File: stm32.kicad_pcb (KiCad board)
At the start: 4 copper layers, 50 x 100 mm, 165 parts, among them CN1 SM04B-SRSS-TB (LF)(SN), CN2 SM04B-SRSS-TB (LF)(SN), CN3 SM04B-SRSS-TB (LF)(SN), J1 PZ254V-11-03P_C2937625, J2 PZ254V-11-03P_C2937625, J3 B2B-PH-SM4-TB (LF)(SN), J5 PZ254V-11-03P_C2937625, P1 TYPE-C 16PIN 2MD(073), Q1 DMG2301L-7, SW1 JS102011JCQN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

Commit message: pre placement and type c routing
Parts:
- moved P1 149.8 mm to (60.0, 128.5)
- moved D7 146.7 mm to (53.5, 125.6), turned to 90 degrees
- moved D4 142.8 mm to (73.5, 128.0), turned to -90 degrees
- moved D3 141.5 mm to (76.5, 127.8), turned to -90 degrees
- moved R35 139.6 mm to (52.5, 106.5), turned to -90 degrees
- moved D9 139.0 mm to (57.5, 121.0)
- moved D6 137.3 mm to (66.5, 127.4), turned to 90 degrees
- moved D8 136.5 mm to (61.4, 121.0), turned to 180 degrees
- moved R37 135.9 mm to (55.5, 106.5), turned to -90 degrees
- moved R7 134.7 mm to (51.8, 122.5)
- moved U6 134.1 mm to (66.5, 106.5)
- moved C7 129.8 mm to (51.5, 117.5), turned to -90 degrees
- moved U2 129.0 mm to (74.0, 123.5), turned to -90 degrees
- moved C6 128.8 mm to (51.5, 112.5), turned to 90 degrees
- moved TP2 127.9 mm to (52.5, 38.0), turned to 180 degrees
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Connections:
- C1 pad 2: +5V -> /USB/5V_INA
- C133 pad 2: +5V -> /USB/5V_INA
- C134 pad 2: +5V -> /USB/5V_INA
- R1 pad 2: +5V -> /USB/5V_INA
- R33 pad 1: /stm32_page/RGB_LEDS -> /stm32_page/RGB_LEDS_R
- R41 pad 1: /stm32_page/SWDIO -> /stm32_page/SWCLK
- U1 pad 28: /stm32_page/RGB_LEDS -> /stm32_page/RGB_LEDS_R
- U3 pad 1: +5V -> /USB/5V_INA
- U5 pad 3: Net-(U5-VIN) -> +5V
- U6 pad 1: +5V -> /USB/5V_INA
- U6 pad 10: +5V -> /USB/5V_INA
- U6 pad 12: +5V -> /USB/5V_INA
- U6 pad 14: Net-(U5-VIN) -> +5V
- U6 pad 15: Net-(U5-VIN) -> +5V
- U6 pad 16: Net-(U5-VIN) -> +5V
- U6 pad 2: +5V -> /USB/5V_INA
- U6 pad 3: +5V -> /USB/5V_INA
- U9 pad 2: /stm32_page/RGB_LEDS -> /sensors/DIN
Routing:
- net +5VP: track 0.00 -> 34.6 mm, vias 0 -> 10
- net GND: track 0.00 -> 19.1 mm, vias 0 -> 13
- net /USB/USB_TX: track 0.00 -> 14.5 mm, vias 0 -> 2
- net /USB/USB_RX: track 0.00 -> 13.6 mm, vias 0 -> 2
- net /USB/CC2: track 0.00 -> 11.6 mm
- net /USB/STAT2: track 0.00 -> 9.44 mm
- net Net-(U13-V3): track 0.00 -> 8.84 mm
- net /USB/CC1: track 0.00 -> 8.22 mm
- net /USB/STAT1: track 0.00 -> 7.70 mm
- net Net-(D3-A): track 0.00 -> 1.95 mm
- net Net-(D4-A): track 0.00 -> 1.75 mm
- added copper zone on In2.Cu, net +3V3
- added copper zone on In2.Cu, net +5V
- added copper zone on In2.Cu, net +5VP
- added copper zone on In1.Cu, net GND

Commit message: routing - type c and all 5vp+ cmp
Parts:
- moved D9 0.50 mm to (58.0, 121.0)
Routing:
- net /USB/USB_D-: track 0.00 -> 14.4 mm, vias 0 -> 2
- net /USB/USB_D+: track 0.00 -> 11.7 mm
- net GND: track 19.1 -> 22.6 mm, vias 13 -> 15

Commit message: routing all power
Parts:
- added C8: CC0603KRX7R9BB104, easyeda2kicad:C0603, F.Cu at (71.0, 108.7)
- moved D1 25.5 mm to (96.0, 130.0)
- moved R44 24.7 mm to (95.6, 110.2), turned to 180 degrees
- moved R43 23.4 mm to (93.5, 112.0), turned to 180 degrees
- moved R2 20.0 mm to (98.0, 127.0), turned to 90 degrees
- moved R3 19.0 mm to (87.5, 122.2), turned to -90 degrees
- moved R4 18.6 mm to (82.5, 124.5)
- moved R13 18.1 mm to (95.6, 108.2), turned to 180 degrees
- moved TH1 16.8 mm to (85.5, 122.2), turned to 90 degrees
- moved C2 16.3 mm to (89.0, 112.5), turned to 0 degrees
- moved R16 15.9 mm to (79.5, 127.5), turned to 90 degrees
- moved U3 14.4 mm to (90.6, 109.8), turned to -90 degrees
- moved C4 14.1 mm to (79.2, 123.0), turned to 180 degrees
- moved R8 12.7 mm to (82.5, 127.8)
- moved R9 12.7 mm to (82.5, 131.2)
- moved R1 12.6 mm to (92.6, 107.2), turned to 90 degrees
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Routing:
- net GND: track 22.6 -> 65.3 mm, vias 15 -> 36
- net /stm32_page/I2C3_SDA: track 0.00 -> 35.1 mm
- net /USB/5V_INA: track 0.00 -> 34.4 mm, vias 0 -> 9
- net /stm32_page/I2C3_SCL: track 0.00 -> 28.1 mm
- net LIPO+: track 0.00 -> 18.8 mm, vias 0 -> 6
- net /USB/VIN: track 0.00 -> 10.9 mm, vias 0 -> 4
- net +3V3: track 0.00 -> 9.68 mm, vias 0 -> 5
- net +5V: track 0.00 -> 9.20 mm, vias 0 -> 5
- net Net-(R3-Pad2): track 0.00 -> 7.16 mm
- net Net-(U2-THERM): track 0.00 -> 6.75 mm
- net /USB/P_MODE: track 0.00 -> 6.48 mm
- net Net-(U2-PROG): track 0.00 -> 5.75 mm
- net /USB/raw_voltage: track 0.00 -> 5.30 mm, vias 0 -> 4
- net Net-(U3-FB): track 0.00 -> 4.57 mm
- net Net-(U3-LX2): track 0.00 -> 2.74 mm
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- added copper zone on In2.Cu, net /USB/5V_INA
- added copper zone on In2.Cu, net /USB/VIN
- added copper zone on In2.Cu, net /USB/raw_voltage
- added copper zone on In2.Cu, net LIPO+

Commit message: all done except rgb leds and i2c sns
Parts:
- C44, C45, R28, R29, X1: moved to B.Cu
- moved LED7 99.8 mm to (68.5, 45.0)
- moved LED5 26.1 mm to (72.0, 48.5)
- moved LED6 23.6 mm to (68.5, 48.5)
- moved LED4 20.6 mm to (75.5, 48.5)
- moved R30 19.2 mm to (55.5, 58.5)
- moved LED3 15.5 mm to (79.0, 48.5)
- moved R41 14.2 mm to (83.0, 97.0), turned to 90 degrees
- moved R42 13.5 mm to (94.5, 91.0), turned to 90 degrees
- moved R40 12.7 mm to (84.5, 100.0)
- moved R34 12.0 mm to (85.0, 97.0), turned to -90 degrees
- moved LED2 11.5 mm to (82.5, 48.5)
- moved SW2 9.50 mm to (55.5, 53.5), turned to 180 degrees
- moved R31 8.50 mm to (58.5, 40.0)
- moved D2 8.28 mm to (70.5, 86.2), turned to 90 degrees
- moved SW3 7.50 mm to (55.5, 45.5)
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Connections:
- U9 pad 2: /sensors/DIN -> /stm32_page/RGB_LEDS
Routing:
- net /stm32_page/PB_SW1: track 0.00 -> 60.5 mm, vias 0 -> 2
- net /stm32_page/SWDIO: track 0.00 -> 53.3 mm, vias 0 -> 2
- net /stm32_page/SWCLK: track 0.00 -> 52.4 mm, vias 0 -> 2
- net /USB/RXD_0: track 1.46 -> 47.9 mm, vias 1 -> 2
- net +3V3: track 9.68 -> 53.7 mm, vias 5 -> 18
- net /USB/TXD_0: track 1.25 -> 44.0 mm, vias 1 -> 2
- net GND: track 65.3 -> 105.7 mm, vias 36 -> 63
- net /stm32_page/STM32_NRST: track 0.00 -> 40.2 mm, vias 0 -> 2
- net /stm32_page/I2C3_SDA: track 35.1 -> 73.3 mm, vias 0 -> 2
- net /stm32_page/UART2_RX: track 0.00 -> 38.1 mm
- net /stm32_page/PWM_CH1: track 0.00 -> 34.5 mm
- net /stm32_page/UART2_TX: track 0.00 -> 27.1 mm
- net /stm32_page/MAX3221_RX_OUT: track 0.00 -> 26.6 mm
- net /stm32_page/PWM_CH4: track 0.00 -> 25.8 mm
- net /stm32_page/I2C3_SCL: track 28.1 -> 51.5 mm, vias 0 -> 2
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
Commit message: all done except rgb leds (to finish) and i2c sns
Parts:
- C10, C11, C12, C13: moved to B.Cu
- moved LED8 91.7 mm to (72.0, 45.0), turned to 180 degrees
- moved C13 29.8 mm to (72.0, 48.5), turned to 0 degrees
- moved C12 24.4 mm to (75.5, 48.5), turned to 0 degrees
- moved C11 19.3 mm to (79.0, 48.5), turned to 0 degrees
- moved C10 15.0 mm to (82.5, 48.5), turned to 0 degrees
- turned LED7 to 180 degrees
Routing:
- net +5V: track 9.20 -> 20.0 mm, vias 5 -> 12
- net GND: track 105.7 -> 114.7 mm, vias 63 -> 68
- net Net-(LED6-DO): track 0.00 -> 5.49 mm
- net Net-(LED7-DO): track 0.00 -> 2.12 mm
- net Net-(LED5-DO): track 0.00 -> 2.12 mm
- net Net-(LED4-DO): track 0.00 -> 2.12 mm
- net Net-(LED3-DO): track 0.00 -> 2.12 mm
- net Net-(LED2-DO): track 0.00 -> 2.09 mm

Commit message: RGB leds done
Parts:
- C14, C15, C16, C17, C18, C19, C20, C21, C22, C23, C24, C25, C26, C27, C28, C29, C30, C31, C32, C33, C34: moved to B.Cu
- moved LED9 95.7 mm to (74.6, 47.8), turned to 180 degrees
- moved LED12 92.3 mm to (81.6, 44.3)
- moved LED13 87.8 mm to (78.1, 44.3)
- moved LED10 86.1 mm to (78.1, 47.8), turned to 180 degrees
- moved LED11 84.5 mm to (81.6, 47.8), turned to 180 degrees
- moved LED17 83.7 mm to (67.6, 40.8), turned to 180 degrees
- moved LED14 83.3 mm to (74.6, 44.3)
- moved LED22 83.0 mm to (81.6, 37.3)
- moved LED18 81.1 mm to (71.1, 40.8), turned to 180 degrees
- moved LED15 78.9 mm to (71.1, 44.3)
- moved LED19 78.8 mm to (74.6, 40.8), turned to 180 degrees
- moved LED23 78.6 mm to (78.1, 37.3)
- moved C17 78.1 mm to (75.5, 46.8), turned to 180 degrees
- moved C18 77.4 mm to (79.0, 47.0), turned to 180 degrees
- moved C19 76.7 mm to (82.5, 47.0), turned to 180 degrees
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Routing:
- net GND: track 114.7 -> 157.2 mm, vias 68 -> 88
- net +5V: track 20.0 -> 62.1 mm, vias 12 -> 30
- net Net-(LED21-DO): track 0.00 -> 5.78 mm
- net Net-(LED11-DO): track 0.00 -> 5.23 mm
- net Net-(LED16-DO): track 0.00 -> 5.16 mm
- net Net-(LED8-DO): track 0.00 -> 2.12 mm
- net Net-(LED25-DO): track 0.00 -> 2.12 mm
- net Net-(LED24-DO): track 0.00 -> 2.12 mm
- net Net-(LED23-DO): track 0.00 -> 2.12 mm
- net Net-(LED22-DO): track 0.00 -> 2.12 mm
- net Net-(LED20-DO): track 0.00 -> 2.12 mm
- net Net-(LED19-DO): track 0.00 -> 2.12 mm
- net Net-(LED18-DO): track 0.00 -> 2.12 mm
- net Net-(LED17-DO): track 0.00 -> 2.12 mm
- net Net-(LED15-DO): track 0.00 -> 2.12 mm
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
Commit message: i2c sns done - all done
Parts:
- moved R38 12.3 mm to (90.0, 50.5), turned to 180 degrees
- moved C36 10.2 mm to (87.5, 64.5)
- moved C52 10.2 mm to (87.5, 61.0)
- moved TP1 10.0 mm to (95.5, 49.0)
- moved C51 9.82 mm to (83.5, 60.0)
- moved U8 9.71 mm to (83.5, 63.0)
- moved C5 9.22 mm to (77.5, 58.5)
- moved U4 9.22 mm to (74.0, 58.5)
- moved U9 7.81 mm to (90.0, 54.0)
- moved C37 6.36 mm to (87.0, 52.5), turned to 90 degrees
- moved R31 3.04 mm to (55.5, 40.5)
- moved R39 2.00 mm to (58.5, 37.0)
- moved TP2 1.80 mm to (54.0, 37.0)
- moved C25 1.64 mm to (67.5, 40.8)
- moved C28 1.64 mm to (78.0, 40.8)
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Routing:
- net GND: track 157.2 -> 191.9 mm, vias 88 -> 125
- net /stm32_page/RGB_LEDS: track 0.00 -> 28.2 mm
- net /sensors/SCL: track 0.00 -> 26.9 mm
- net /sensors/SDA: track 6.35 -> 32.8 mm, vias 0 -> 3
- net +3V3: track 53.7 -> 77.1 mm, vias 18 -> 28
- net /stm32_page/IMU_INT: track 15.9 -> 29.8 mm, vias 1 -> 2
- net /sensors/led_matrix/DIN: track 0.00 -> 13.0 mm
- net /stm32_page/SYS_WKUP1: track 17.7 -> 30.1 mm, vias 1 -> 2
- net Net-(LED26-DO): track 0.00 -> 7.53 mm
- net Net-(LED2-DI): track 0.00 -> 7.29 mm
- net Net-(D2-A): track 0.00 -> 4.86 mm
- net Net-(D10-A): track 0.00 -> 4.86 mm
- net Net-(D11-A): track 0.00 -> 4.57 mm
- net /sensors/led_matrix/DOUT: track 0.00 -> 4.46 mm
- net Net-(D1-A): track 0.00 -> 3.16 mm
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
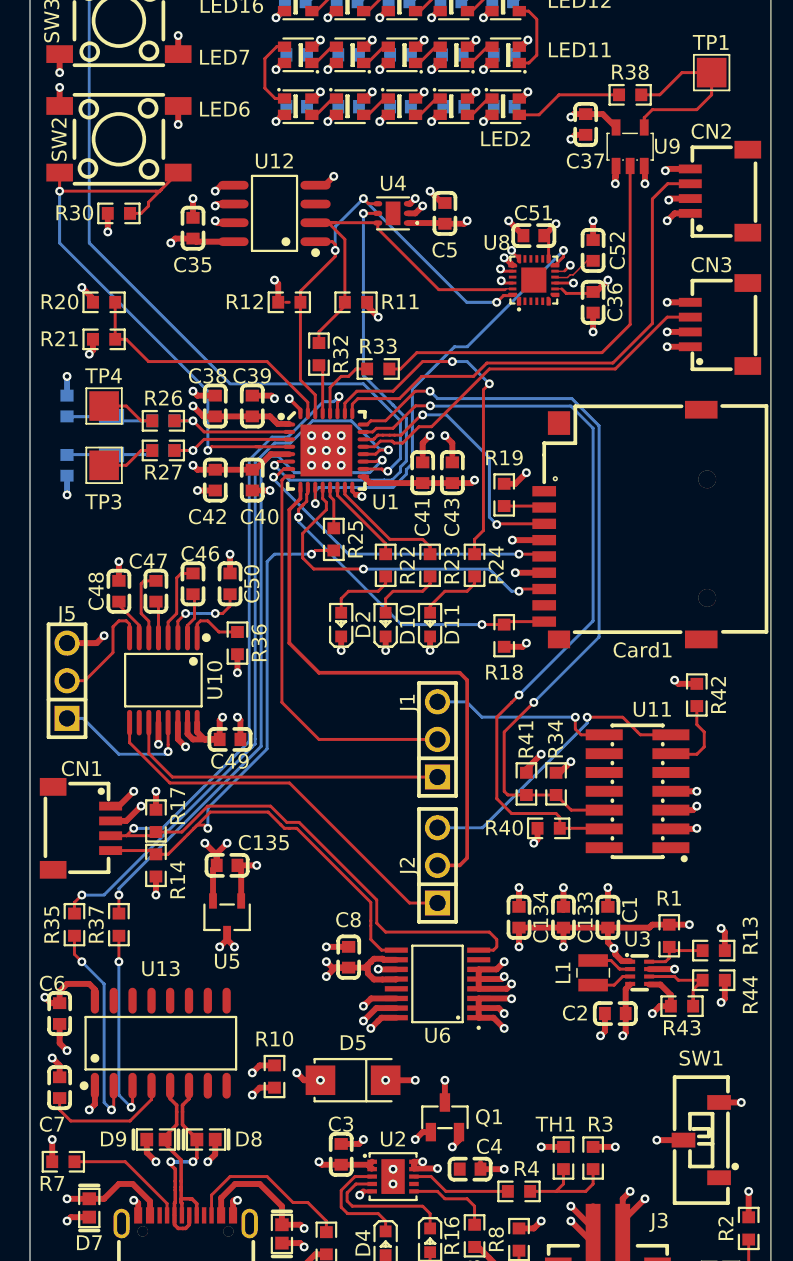
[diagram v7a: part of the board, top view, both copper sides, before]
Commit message: fix DRC except via size to all
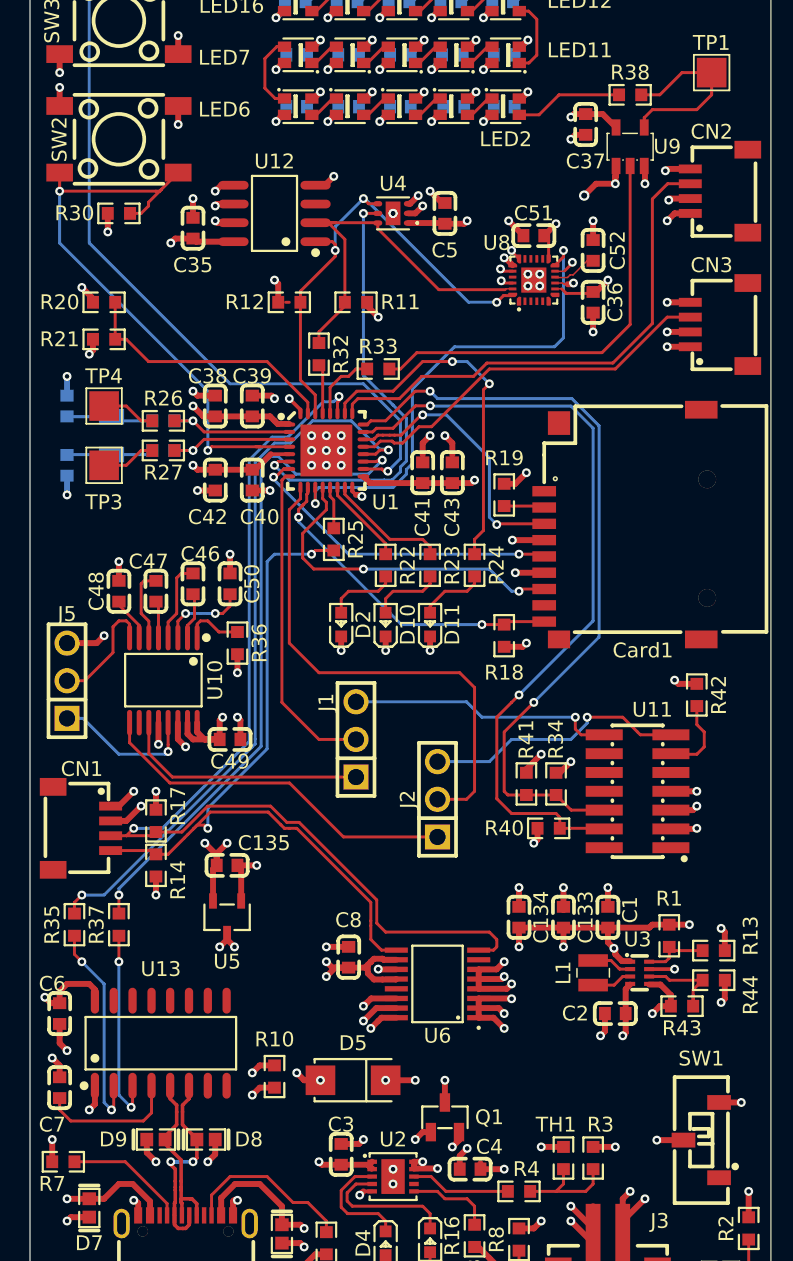
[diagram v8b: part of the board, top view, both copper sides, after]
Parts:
- moved J1 5.50 mm to (71.5, 94.0)
- moved J2 4.46 mm to (77.0, 98.0)
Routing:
- net /stm32_page/UART2_TX: track 27.1 -> 21.6 mm
- net /stm32_page/MAX3221_TX_IN: track 22.2 -> 16.7 mm
- net /stm32_page/VCP_TX: track 12.8 -> 18.3 mm
- net /stm32_page/UART2_RX: track 38.1 -> 34.3 mm
- net /stm32_page/IMU_INT: track 29.8 -> 33.2 mm
- net GND: track 191.9 -> 194.9 mm, vias 125 -> 132
- net /stm32_page/MAX3221_RX_OUT: track 26.6 -> 24.8 mm
- net /stm32_page/VCP_RX: track 19.6 -> 17.7 mm
- net LIPO+: track 18.8 -> 20.4 mm, vias 6 -> 7
- net Net-(U13-V3): track 8.84 -> 9.37 mm
